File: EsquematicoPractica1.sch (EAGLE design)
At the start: 94 parts, among them IC1 GSOT05C-GS08, IC2 RCV420JP, IC3 TC7662BEOA, IC4 MC7812BTG, IC5 RCV420JP, IC6 TC7662BEOA, IC7 MC7812BTG, J1 M50-3500542, Q1 IRF7416PBF, Q2 IRF7416PBF, U1 MKL27Z64VLH4, U13 TLV274QPWRG4Q1, U2 SFH6156-4TSMD-4_VO-L, U3 MC34063ADR, U4 SFH6156-4TSMD-4_VO-L, U5 SFH6156-4TSMD-4_VO-L, U6 SFH6156-4TSMD-4_VO-L, X1 MINI-USB-SCHIELD-32005-201, Y3 32.768KHZ

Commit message: Con todo
Revisar un montaje de 5V a 3V3 en openSDA interface, algunas resistencias y terminar de conectar el open SDA Interface con la KL.
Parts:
- removed J1: M50-3500542, M50-3500542:M50-3500542
- removed OUT1, OUT2: (no value), con-ptr500:AK300/2
- removed R102: 10K, rcl:R-US_M1206
- added C23, C24: 0402ZD105KAT2A, 0402ZD105KAT2A:0402ZD105KAT2A
- added C25, C26: 04025A220JAT2A, 04025A220JAT2A:04025A220JAT2A
- added C27: C0402C104K8PAC, C0402C104K8PAC:C0402C104K8PAC
- added C28: 0.33u, rcl:C-USC0805
- added C29: 0.1u, rcl:C-USC0805
- added IC8: GSOT05C-GS08, GSOT05C-GS08:GSOT05C-GS08
- added IC9: (no value), v-reg:78XXL
- added J2, J3: M50-3500542, M50-3500542:M50-3500542
- added JP1, JP2, JP3, JP4: (no value), pinhead:PINHD-1X2/90
- added JP5: (no value), pinhead:PINHD-1X2
- added L3, L4: MPZ2012S331A, MPZ2012S331AT000:MPZ2012S331AT000
- added R21, R22: 33, RC0402FR-0733RL:RC0402FR-0733RL
- added R23, R24, R25, R28: RK73B1JLTD103J, RK73B1JLTD103J:RK73B1JLTD103J
- added R26: CRCW06034K70JNEA, CRCW06034K70JNEA:CRCW06034K70JNEA
- added R27: 10K, rcl:R-US_M1206
- added S2: EVQPE105K, EVQPE105K:EVQPE105K
- added U10, U8, U9: 74LVC125AD, 74LVC125ADB:74LVC125AD
- added U7: MK20DX128VFM5, MK20DX128VFM5:MK20DX128VFM5
- added X2: MINI-USB-SCHIELD-32005-201, con-cypressindustries:MINI-USB-SCHIELD-32005-201
- added Y1: ABM3B-8.000MHZ-B2-T, ABM3B-8.000MHZ-B2-T:ABM3B-8.000MHZ-B2-T
- R105: value 33 -> 5.7K
- R106: value 33 -> 3.3K
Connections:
- removed net GND_D: R5.2, R7.2
- removed net N$32: R14.1, R16.2
- removed net N$43: R18.1, R19.2
- removed net N$75: U13.2IN-, U13.2OUT
- removed net N$77: U13.4IN-, U13.4OUT
- removed net PINOUT_D0: U2.A
- removed net PINOUT_D1: U4.A
- removed net PTA20: C5.1, C6.2, S1.2, U1.PTA20
- new net ADC0_DM0_IN_A4-20: R18.1, R19.2, U1.PTE21
- new net ADC0_DP3_IN_A4-20: R14.1, R16.2, U1.PTE22
- new net I2C0_SCL: U$1.SCL, U1.PTE24
- new net I2C0_SDA: U$1.SDA, U1.PTE25
- new net KL27_SWD_CLK: JP4.1
- new net LPUART0_RX: U$1.RX, U1.PTA1
- new net LPUART0_TX: U$1.TX, U1.PTA2
- new net N$46: IC8.CATHODE(2), R21.1, X2G$1.3
- new net N$47: L3.1, X2G$1.1
- new net N$48: IC8.CATHODE(1), R22.1, X2G$1.2
- new net N$49: L4.1, X2S.S1, X2S.S2, X2S.S3, X2S.S4
- new net N$50: C23.1
- new net N$51: C25.1, U7.PTA19, Y1.NC(1)
- new net N$52: U8.GND
- new net N$53: U7.PTD4/LLWU_P14
- new net N$54: JP2.2, U10.4Y
- new net N$55: R25.1, R26.2, U7.PTD7
- new net N$56: R25.2
- new net N$57: C27.2
- new net N$58: JP1.2, U8.1Y, U9.3A
- new net N$59: J3.2
- new net P3V3_JMP2: R28.1
- new net P3V3_KL27Z: J3.1
- new net PIN_INT: U$1.INT, U1.PTE16
- new net PTA20_RST: C5.1, C6.2, S1.2, U$1.RST, U1.PTA20
- new net PTA3_IN_OA: U1.PTA3, U13.2IN-, U13.2OUT
- new net PTA4_IN_OA: U1.PTA4, U13.4IN-, U13.4OUT
- new net PTE0_D1_IN: R12.2, U1.PTE0, U6.C
- new net PTE1_D2_IN: R13.2, U1.PTE1, U5.C
- new net PTE20_A0: U$1.AN, U1.PTE20
- new net PTE30_D1_OUT: U1.PTE30, U4.A
- new net PTE31_D2_OUT: U1.PTE31, U2.A
- new net RST_K20D50_B: C27.1, JP3.2, R28.2, S2.1
- new net SDA_P17: C26.1, U7.PTA18, Y1.NC(2)
- new net SDA_P20: R23.1, U7.PTB0/LLWU_P5, U8.!_2
- new net SDA_P21: JP3.1, U7.PTB1
- new net SDA_P26: U10.4A, U7.PTC5/LLWU_P9
- new net SDA_P27: U7.PTC6/LLWU_P10, U8.1A
- new net SDA_P28: U7.PTC7, U9.3Y
- new net SDA_SWD_EN: R24.2, U10.!, U7.PTA4/LLWU_P3, U9.!_4
- new net SPI0_MISO: U$1.MISO, U1.PTC7
- new net SPI0_MOSI: U$1.MOSI, U1.PTC6/LLWU_P10
- new net SPI0_PCS0: U$1.CS, U1.PTC4/LLWU_P8
- new net SPI0_SCK: U$1.SCK, U1.PTC5/LLWU_P9
- new net SWD_CLK_TGTMCU: J3.4, JP2.1, JP4.2
- new net SWD_DIO_TGTMCU: JP1.1
- new net TPM0_CH2_PWM: U$1.PWM, U1.PTE29
- new net UART1_RX_TGTMCU: U7.PTC4/LLWU_P8
- new net UART1_TX_TGTMCU: U7.PTC3/LLWU_P7
- new net USB_DM1: R22.2, U7.USB0_DM
- new net USB_DP1: R21.2, U7.USB0_DP
- net +3V3: now also U$1.3V3
- net +5V: now also C29.1, IC9.OUT, U$1.5V, U1.VDD, U1.VDD_2, U1.VDD_3
- net EXTAL_32KHZ: now also U1.PTA18
- net GND: now also C24.1, C28.2, C29.2, IC8.ANODE, IC9.GND, J2.3, J2.5, J3.3, L4.2, R5.2, R7.2, S2.2, U$1.GND1, U$1.GND2, U7.VSS, U7.VSSA, X2G$1.5, Y1.GND(2); no longer J1.3, J1.5
- net N$14: now also J3.10
- net N$19: now also JP5.1, R103.1; no longer OUT2-1.KL, R13.2, U5.C
- net N$28: now also JP5.2, R105.1; no longer OUT1-1.KL, R12.2, U6.C
- net N$3: now also Y1.GND(1)
- net N$4: now also C25.2
- net N$7: now also C26.2
- net P3V3_SDA: now also C24.2, J2.1, R23.2, R24.1, R27.2, U7.VDD, U7.VDDA, U8.VCC; no longer J1.1, R102.2
- net P5V_SDA: now also C23.2, L3.2, R26.1
- net SDA_JTAG_TCLK: now also J2.4, U7.PTA0; no longer J1.4
- net SDA_JTAG_TDI: now also J2.8, U7.PTA1; no longer J1.8
- net SDA_JTAG_TDO: now also J2.6, U7.PTA2; no longer J1.6
- net SDA_JTAG_TMS: now also J2.2, R27.1, U7.PTA3; no longer J1.2, R102.1
- net SDA_RST_B: now also J2.10; no longer J1.10
- net VCC: now also C28.1, IC9.IN
- net XTAL_32KHZ: now also U1.PTA19
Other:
- note added: "GND_N2"
- note added: "JTAG INTERFACE"
- note added: "OpenSDA Interface"
- note added: "SWD CONNECTOR"
- note added: "Salida 5V"
- note added: "Target MCU INTERFACE SIGNALS"
- note removed: "OpenSDA INTERFACE JTAG CONNECTOR"
- moved on the sheet: C1, C2, C3, C4, C42, C43, D1, IC1, L1, L2, L5, L6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

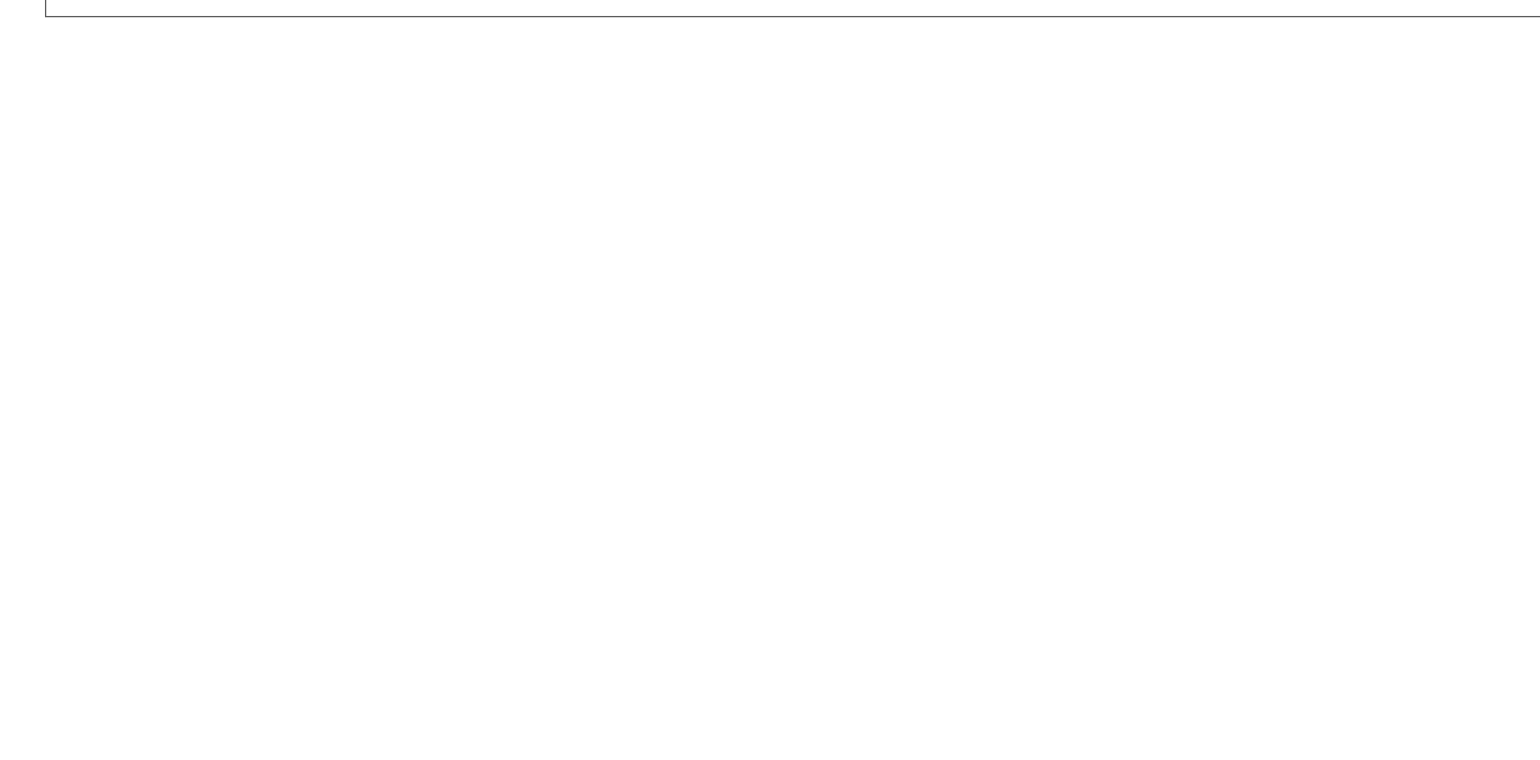
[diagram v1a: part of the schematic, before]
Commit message: Todo falta revisar conexiones
Autoroutear y organizar
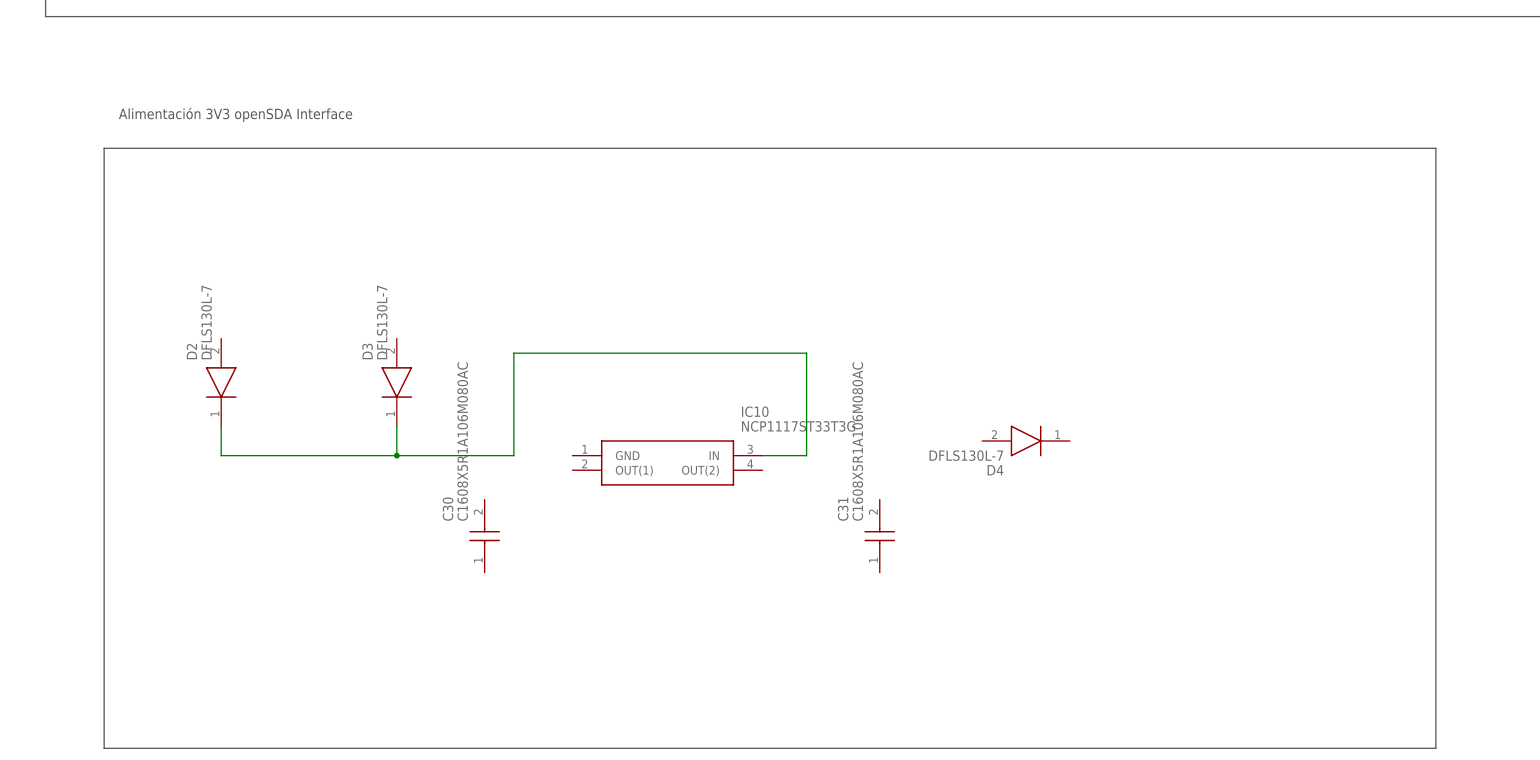
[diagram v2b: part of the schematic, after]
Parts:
- added C30, C31: C1608X5R1A106M080AC, C1608X5R1A106M080AC:C1608X5R1A106M080AC
- added D2, D3, D4: DFLS130L-7, DFLS130L-7:DFLS130L-7
- added IC10: NCP1117ST33T3G, NCP1117ST33T3G:NCP1117ST33T3G
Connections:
- new net N$32: D2.K, D3.K, IC10.IN
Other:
- note added: "Alimentación 3V3 openSDA Interface"
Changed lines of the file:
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@@
 <part name="GND9" library="supply1" library_urn="urn:adsk.eagle:library:371" deviceset="GND" device=""/>
 <part name="JP5" library="pinhead" library_urn="urn:adsk.eagle:library:325" deviceset="PINHD-1X2" device="" package3d_urn="urn:adsk.eagle:package:22435/2"/>
+<part name="D2" library="DFLS130L-7" deviceset="DFLS130L-7" device=""/>
+<part name="D3" library="DFLS130L-7" deviceset="DFLS130L-7" device=""/>
+<part name="IC10" library="NCP1117ST33T3G" deviceset="NCP1117ST33T3G" device=""/>
+<part name="D4" library="DFLS130L-7" deviceset="DFLS130L-7" device=""/>
+<part name="C30" library="C1608X5R1A106M080AC" deviceset="C1608X5R1A106M080AC" device=""/>
+<part name="C31" library="C1608X5R1A106M080AC" deviceset="C1608X5R1A106M080AC" device=""/>
 </parts>
 <sheets>
@@
 <text x="-127" y="-68.58" size="1.778" layer="97">GND_N2</text>
 <text x="45.72" y="-66.04" size="1.778" layer="97">GND_N2</text>
+<wire x1="294.64" y1="-248.92" x2="525.78" y2="-248.92" width="0.1524" layer="97"/>
+<wire x1="525.78" y1="-248.92" x2="525.78" y2="-353.06" width="0.1524" layer="97"/>
+<wire x1="525.78" y1="-353.06" x2="294.64" y2="-353.06" width="0.1524" layer="97"/>
+<wire x1="294.64" y1="-353.06" x2="294.64" y2="-248.92" width="0.1524" layer="97"/>
+<text x="297.18" y="-243.84" size="1.778" layer="97">Alimentación 3V3 openSDA Interface</text>
 </plain>
 <instances>
@@
 <instance part="GND9" gate="1" x="104.14" y="-73.66"/>
 <instance part="JP5" gate="G$1" x="436.88" y="99.06"/>
+<instance part="D2" gate="G$1" x="314.96" y="-297.18" rot="R90"/>
+<instance part="D3" gate="G$1" x="345.44" y="-297.18" rot="R90"/>
+<instance part="IC10" gate="G$1" x="375.92" y="-302.26"/>
+<instance part="D4" gate="G$1" x="462.28" y="-299.72" rot="R180"/>
+<instance part="C30" gate="G$1" x="360.68" y="-322.58" rot="R90"/>
+<instance part="C31" gate="G$1" x="429.26" y="-322.58" rot="R90"/>
 </instances>
 <busses>
@@
 </segment>
 </net>
+<net name="N$32" class="0">
+<segment>
+<pinref part="IC10" gate="G$1" pin="IN"/>
+<wire x1="408.94" y1="-302.26" x2="416.56" y2="-302.26" width="0.1524" layer="91"/>
+<wire x1="416.56" y1="-302.26" x2="416.56" y2="-284.48" width="0.1524" layer="91"/>
+<wire x1="416.56" y1="-284.48" x2="365.76" y2="-284.48" width="0.1524" layer="91"/>
+<wire x1="365.76" y1="-284.48" x2="365.76" y2="-302.26" width="0.1524" layer="91"/>
+<wire x1="365.76" y1="-302.26" x2="345.44" y2="-302.26" width="0.1524" layer="91"/>
+<pinref part="D3" gate="G$1" pin="K"/>
+<wire x1="345.44" y1="-302.26" x2="345.44" y2="-297.18" width="0.1524" layer="91"/>
+<pinref part="D2" gate="G$1" pin="K"/>
+<wire x1="314.96" y1="-297.18" x2="314.96" y2="-302.26" width="0.1524" layer="91"/>
+<wire x1="314.96" y1="-302.26" x2="345.44" y2="-302.26" width="0.1524" layer="91"/>
+<junction x="345.44" y="-302.26"/>
+</segment>
+</net>

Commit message: [Code] Full Esquemático
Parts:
- removed C5, C6: C0402C104K8PAC, C0402C104K8PAC:C0402C104K8PAC
- removed S1: EVQPE105K, EVQPE105K:EVQPE105K
- added JP6: (no value), pinhead:PINHD-1X2/90
- added R29, R30: RK73Z1JTTD, RK73Z1JTTD:RK73Z1JTTD
- R4, R6: value (none) -> 10K
- R5, R7: value (none) -> 1.1K
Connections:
- removed net LPUART0_RX: U$1.RX, U1.PTA1
- removed net LPUART0_TX: U$1.TX, U1.PTA2
- removed net N$59: J3.2
- removed net PTA3_IN_OA: U1.PTA3, U13.2IN-, U13.2OUT
- removed net PTA4_IN_OA: U1.PTA4, U13.4IN-, U13.4OUT
- new net LPUART0_RX_MKB: U$1.RX, U1.PTD6/LLWU_P15
- new net LPUART0_TX_MKB: U$1.TX, U1.PTD7
- new net N$43: C31.2, D4.A, IC10.OUT(1), IC10.OUT(2), R29.1
- new net N$62: C30.1
- new net N$63: D4.K, JP6.1, R29.2, R30.1
- new net N$69: IC10.GND
- new net P5V_KL27Z: D3.A, L5.2, TP5.1
- new net PTB1_IN_OA: U1.PTB1, U13.2IN-, U13.2OUT
- new net PTB2_IN_OA: U1.PTB2, U13.4IN-, U13.4OUT
- net +3V3: no longer C5.2
- net GND: now also C31.1; no longer C6.1, S1.1
- net KL27_SWD_CLK: now also U1.PTA0
- net N$14: no longer J3.10
- net N$32: now also C30.2
- net P3V3_SDA: now also JP6.2, R30.2
- net P5V_SDA: now also D2.A; no longer L5.2, TP5.1
- net PTA20_RST: no longer C5.1, C6.2, S1.2, U1.PTA20
- net RST_K20D50_B: now also J3.10, U1.PTA20
- net SWD_DIO_TGTMCU: now also J3.2, U1.PTA4
- net UART1_RX_TGTMCU: now also U1.PTA1
- net UART1_TX_TGTMCU: now also U1.PTA2
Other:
- note removed: "Pulsador de RST"

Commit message: Esquemático full ahora sí
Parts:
- R10, R8: value 300 -> 220
- R11, R9: value 300 -> 130
- R12, R13: value (none) -> 10K
- R5, R7: value 1.1K -> 10K
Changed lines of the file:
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@@
 <part name="+3V3" library="supply2" library_urn="urn:adsk.eagle:library:372" deviceset="+5V" device="" value="+3V3"/>
 <part name="R4" library="rcl" library_urn="urn:adsk.eagle:library:334" deviceset="R-US_" device="0309/12" package3d_urn="urn:adsk.eagle:package:23571/1" value="10K"/>
-<part name="R5" library="rcl" library_urn="urn:adsk.eagle:library:334" deviceset="R-US_" device="0309/12" package3d_urn="urn:adsk.eagle:package:23571/1" value="1.1K"/>
+<part name="R5" library="rcl" library_urn="urn:adsk.eagle:library:334" deviceset="R-US_" device="0309/12" package3d_urn="urn:adsk.eagle:package:23571/1" value="10K"/>
 <part name="CARGA" library="con-ptr500" library_urn="urn:adsk.eagle:library:181" deviceset="AK300/2" device="" package3d_urn="urn:adsk.eagle:package:9881/1"/>
 <part name="+24V" library="con-ptr500" library_urn="urn:adsk.eagle:library:181" deviceset="AK300/2" device="" package3d_urn="urn:adsk.eagle:package:9881/1"/>
@@
 <part name="Q2" library="IRF7416PBF_Completo" deviceset="IRF7416PBF" device=""/>
 <part name="R6" library="rcl" library_urn="urn:adsk.eagle:library:334" deviceset="R-US_" device="0309/12" package3d_urn="urn:adsk.eagle:package:23571/1" value="10K"/>
-<part name="R7" library="rcl" library_urn="urn:adsk.eagle:library:334" deviceset="R-US_" device="0309/12" package3d_urn="urn:adsk.eagle:package:23571/1" value="1.1K"/>
+<part name="R7" library="rcl" library_urn="urn:adsk.eagle:library:334" deviceset="R-US_" device="0309/12" package3d_urn="urn:adsk.eagle:package:23571/1" value="10K"/>
 <part name="CARGA2" library="con-ptr500" library_urn="urn:adsk.eagle:library:181" deviceset="AK300/2" device="" package3d_urn="urn:adsk.eagle:package:9881/1"/>
 <part name="+24V1" library="con-ptr500" library_urn="urn:adsk.eagle:library:181" deviceset="AK300/2" device="" package3d_urn="urn:adsk.eagle:package:9881/1"/>
 <part name="U6" library="SFH6156-4T" deviceset="SFH6156-4T" device="SMD-4_VO-L"/>
 <part name="INPUT1" library="con-ptr500" library_urn="urn:adsk.eagle:library:181" deviceset="AK300/2" device="" package3d_urn="urn:adsk.eagle:package:9881/1"/>
-<part name="R10" library="rcl" library_urn="urn:adsk.eagle:library:334" deviceset="R-US_" device="0204/7" package3d_urn="urn:adsk.eagle:package:23498/1" value="300"/>
-<part name="R11" library="rcl" library_urn="urn:adsk.eagle:library:334" deviceset="R-US_" device="0309/12" package3d_urn="urn:adsk.eagle:package:23571/1" value="300"/>
+<part name="R10" library="rcl" library_urn="urn:adsk.eagle:library:334" deviceset="R-US_" device="0204/7" package3d_urn="urn:adsk.eagle:package:23498/1" value="220"/>
+<part name="R11" library="rcl" library_urn="urn:adsk.eagle:library:334" deviceset="R-US_" device="0309/12" package3d_urn="urn:adsk.eagle:package:23571/1" value="130"/>
 <part name="LED1" library="led" library_urn="urn:adsk.eagle:library:259" deviceset="LED" device="5MM" package3d_urn="urn:adsk.eagle:package:15799/2"/>
-<part name="R12" library="rcl" library_urn="urn:adsk.eagle:library:334" deviceset="R-US_" device="0204/7" package3d_urn="urn:adsk.eagle:package:23498/1"/>
+<part name="R12" library="rcl" library_urn="urn:adsk.eagle:library:334" deviceset="R-US_" device="0204/7" package3d_urn="urn:adsk.eagle:package:23498/1" value="10K"/>
 <part name="3.3V" library="con-ptr500" library_urn="urn:adsk.eagle:library:181" deviceset="AK300/2" device="" package3d_urn="urn:adsk.eagle:package:9881/1"/>
 <part name="U5" library="SFH6156-4T" deviceset="SFH6156-4T" device="SMD-4_VO-L"/>
 <part name="INPUT2" library="con-ptr500" library_urn="urn:adsk.eagle:library:181" deviceset="AK300/2" device="" package3d_urn="urn:adsk.eagle:package:9881/1"/>
-<part name="R8" library="rcl" library_urn="urn:adsk.eagle:library:334" deviceset="R-US_" device="0309/12" package3d_urn="urn:adsk.eagle:package:23571/1" value="300"/>
-<part name="R9" library="rcl" library_urn="urn:adsk.eagle:library:334" deviceset="R-US_" device="0309/12" package3d_urn="urn:adsk.eagle:package:23571/1" value="300"/>
+<part name="R8" library="rcl" library_urn="urn:adsk.eagle:library:334" deviceset="R-US_" device="0309/12" package3d_urn="urn:adsk.eagle:package:23571/1" value="220"/>
+<part name="R9" library="rcl" library_urn="urn:adsk.eagle:library:334" deviceset="R-US_" device="0309/12" package3d_urn="urn:adsk.eagle:package:23571/1" value="130"/>
 <part name="LED2" library="led" library_urn="urn:adsk.eagle:library:259" deviceset="LED" device="5MM" package3d_urn="urn:adsk.eagle:package:15799/2"/>
-<part name="R13" library="rcl" library_urn="urn:adsk.eagle:library:334" deviceset="R-US_" device="0204/7" package3d_urn="urn:adsk.eagle:package:23498/1"/>
+<part name="R13" library="rcl" library_urn="urn:adsk.eagle:library:334" deviceset="R-US_" device="0204/7" package3d_urn="urn:adsk.eagle:package:23498/1" value="10K"/>
 <part name="3.3V1" library="con-ptr500" library_urn="urn:adsk.eagle:library:181" deviceset="AK300/2" device="" package3d_urn="urn:adsk.eagle:package:9881/1"/>
 <part name="LED3" library="led" library_urn="urn:adsk.eagle:library:259" deviceset="LED" device="5MM" package3d_urn="urn:adsk.eagle:package:15799/2"/>
